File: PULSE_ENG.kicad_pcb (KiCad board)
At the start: 4 copper layers, 142 parts, among them IC1 TPS7B8733QDDARQ1, IC2 TPS7B8750QDDARQ1, IC28 INA226AIDGSR, IC29 TPS25940ARVCR, IC30 TPS25940ARVCR, IC31 INA226AIDGSR, J10 Screw_Terminal_01x01, J11 Screw_Terminal_01x01, J8 Screw_Terminal_01x04, J9 Screw_Terminal_01x06, U1 ATSAMD21J17D-M, U2 LT6108IMS8-1-TRPBF, U3 LM139ADRG4, U4 EPC2152, U5 LT6108IMS8-1-TRPBF

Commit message: Final addings
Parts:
- J11: value Screw_Terminal_01x01 -> Screw_Terminal_01x04; footprint TerminalBlock_Phoenix:TerminalBlock_Phoenix_MKDS-1,5-2-5.08_1x02_P5.08mm_Horizontal -> TerminalBlock_Phoenix:TerminalBlock_Phoenix_MKDS-1,5-4-5.08_1x04_P5.08mm_Horizontal
- moved J11 43.1 mm to (172.0, 61.4)
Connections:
- C3 pad 1: /3.3V -> VDDIN
- C4 pad 1: /3.3V -> VDDIN
- C8 pad 1: Net-(U4-Vdd12F) -> Net-(J11-Pin_3)
- J11 pad 1: /Vout_BUCK -> 12V_1
- J11 pad 2: GND -> /Vout_BUCK
- U1 pad 55: /3.3V -> VDDCORE
- U1 pad 56: /3.3V -> VDDIN
- U4 pad 1: Net-(U4-Vdd12F) -> Net-(J11-Pin_3)
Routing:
- net 12V_1: track 26.5 -> 131.8 mm, vias 3 -> 4
- net Net-(J11-Pin_3): track 0.00 -> 94.6 mm, vias 0 -> 2
- net /Vout_BUCK: track 166.5 -> 207.9 mm
- net Net-(U4-Vdd12F): track 10.7 -> 0.00 mm
- net GND: vias 33 -> 34
- net (no net): vias 1 -> 0
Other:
- board text added: "BUCK pins"
- board text added: "PCU (EPS V4.0) JAN2026 Tom Gourru-Bourgeois"
- board text removed: "BUCK BYPASS Pin"

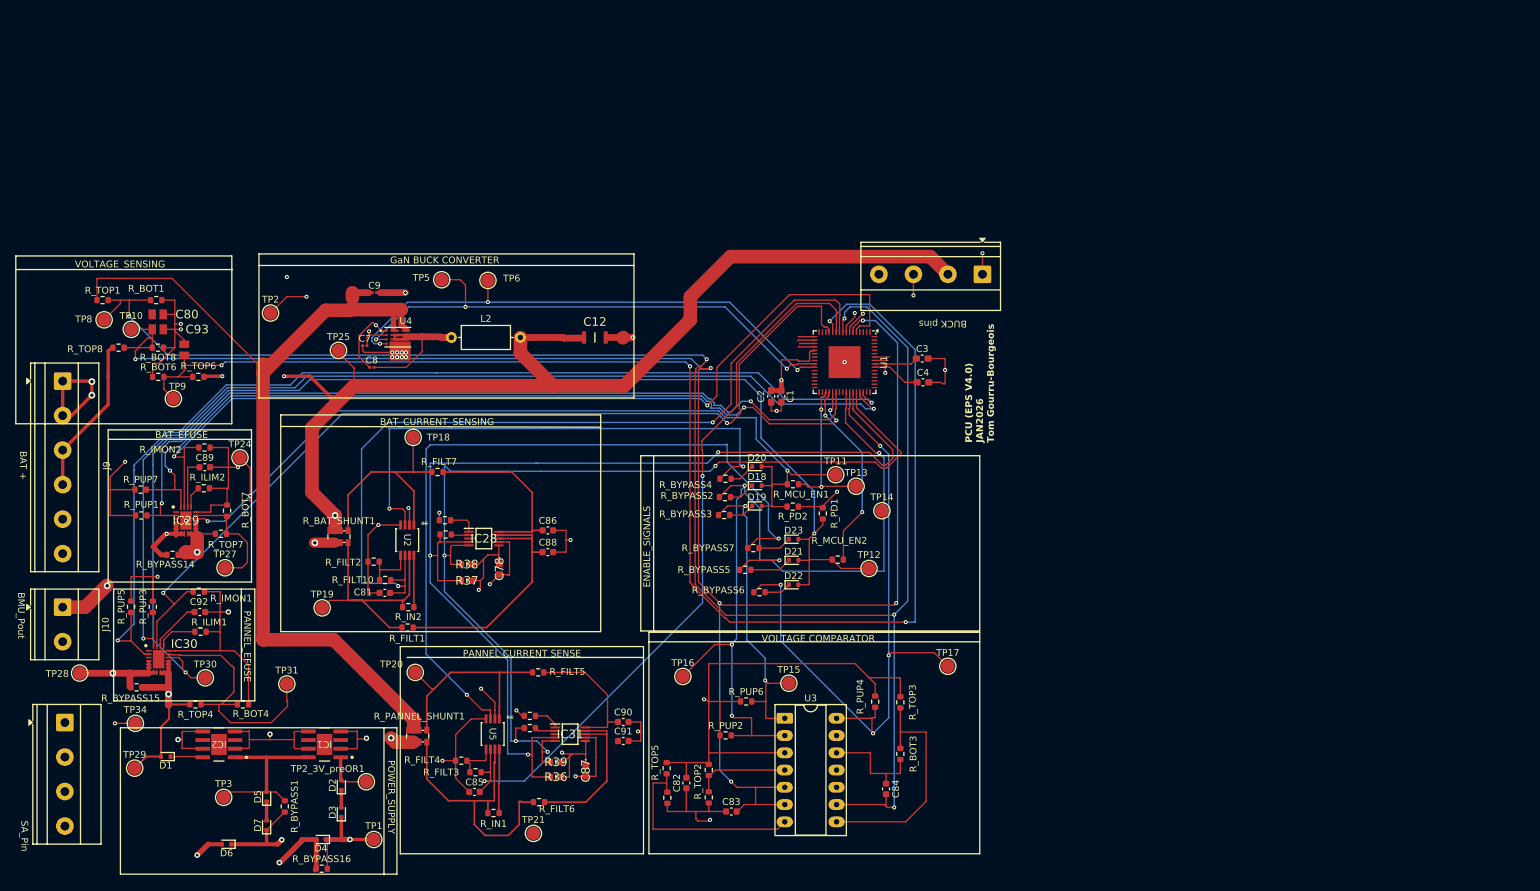
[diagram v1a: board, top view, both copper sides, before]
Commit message: changed 90deg traces, added est logo
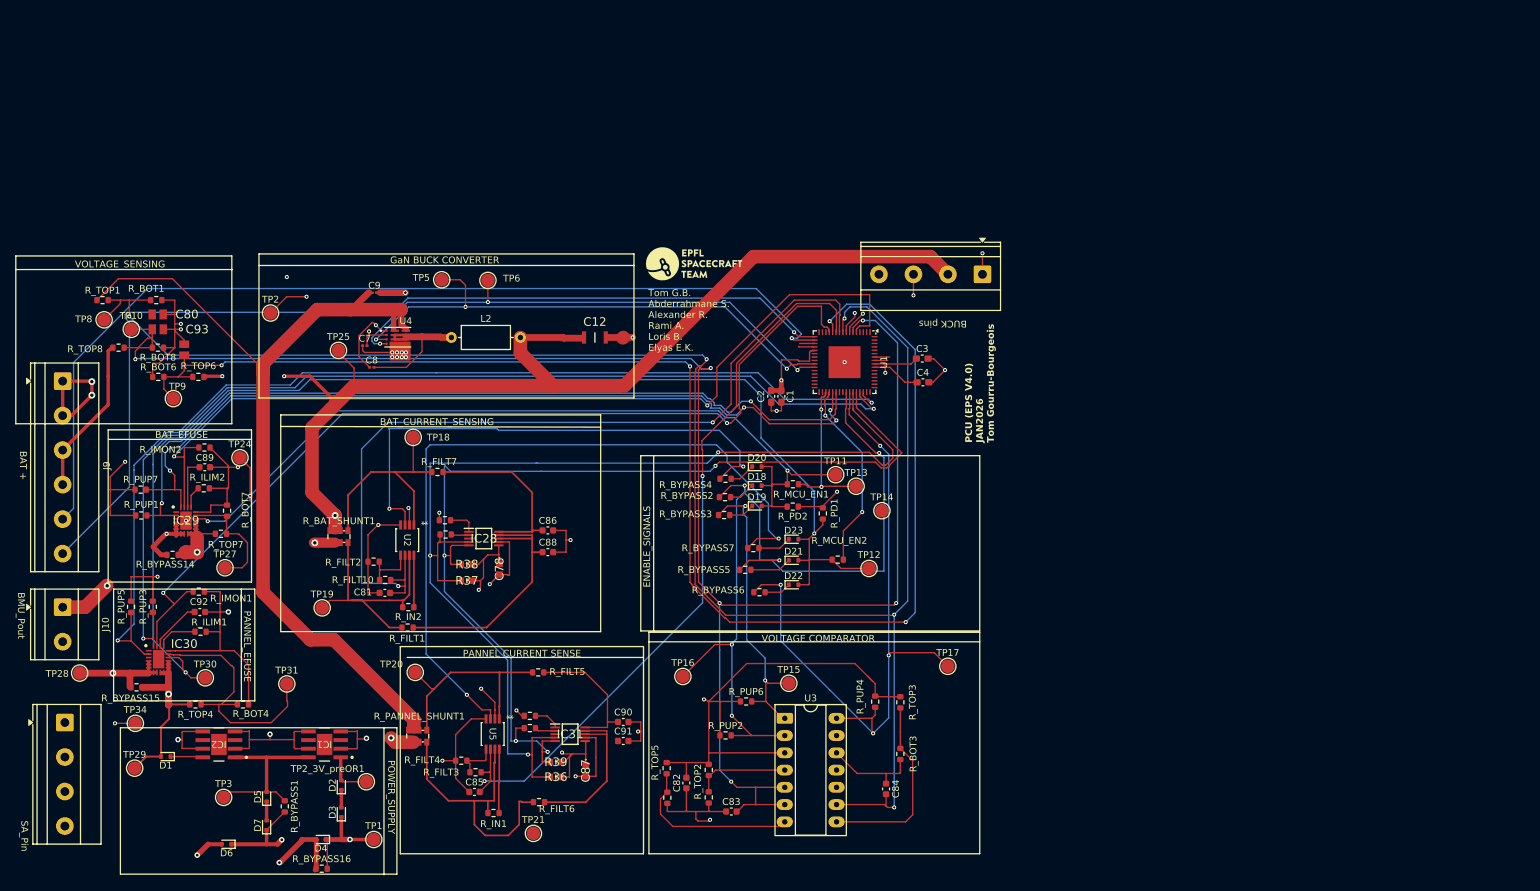
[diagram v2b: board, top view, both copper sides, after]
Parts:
- added G***: LOGO, PULSE_Library:EST_logo_footprint, F.Cu at (129.6, 59.8)
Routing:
- net /HEATER_SWITCH: track 2.40 -> 144.4 mm, vias 0 -> 1
- net /POWER_SWITCH: track 2.54 -> 143.3 mm, vias 0 -> 1
- net /3.3V: track 579.6 -> 569.7 mm
- net /V_pannel_protected: track 138.8 -> 132.0 mm
- net Net-(U3-3IN-): track 34.4 -> 28.1 mm
- net GND: track 282.4 -> 276.6 mm
- net Net-(U3-1IN+): track 31.5 -> 25.9 mm
- net VDDIN: track 0.00 -> 3.34 mm
- net /Vout_BUCK: track 207.9 -> 205.9 mm
- net /PCU_Control/BAT_OVC: track 78.2 -> 76.3 mm
- net /BAT_EFUSE_EN: track 131.5 -> 129.7 mm
- net /BAT_OVP_FLAG: track 129.1 -> 127.6 mm
- net /BAT_UVP_FLAG: track 45.8 -> 44.5 mm
- net /PCU_Control/PANNEL_OVC: track 111.5 -> 110.7 mm
- net /VCHG_RAIL_SENSE: track 212.6 -> 211.7 mm
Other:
- board text added: "Tom G.B. Abderrahmane S. Alexander R. Rami A. Loris B. Elyas E.K."

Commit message: Modofications asked and BOM
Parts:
- D3: value 1N4148WT -> 1N5711; footprint Diode_SMD:D_SOD-523 -> Diode_THT:D_DO-35_SOD27_P7.62mm_Horizontal
- L2: footprint Inductor_THT:L_Axial_L7.0mm_D3.3mm_P10.16mm_Horizontal_Fastron_MICC -> Inductor_SMD:L_0603_1608Metric
- moved R_IN1 17.9 mm to (92.2, 124.6), turned to 90 degrees
- moved TP21 17.6 mm to (90.2, 135.7)
- moved R_IN2 16.8 mm to (80.4, 95.2), turned to 90 degrees
- moved R_FILT1 15.7 mm to (96.7, 100.8), turned to 180 degrees
- moved C81 14.9 mm to (82.8, 93.5), turned to 180 degrees
- moved C85 14.1 mm to (94.5, 123.8), turned to 180 degrees
- moved C88 11.7 mm to (96.4, 103.7), turned to -90 degrees
- moved C86 11.6 mm to (96.6, 97.4)
- moved R_FILT10 11.3 mm to (82.8, 95.2), turned to 180 degrees
- moved R_FILT7 10.1 mm to (96.7, 99.3), turned to 180 degrees
- moved R_FILT3 9.83 mm to (94.5, 125.3), turned to 180 degrees
- moved C91 9.80 mm to (109.6, 132.5)
- moved C90 9.61 mm to (109.5, 126.8)
- moved R_FILT5 9.36 mm to (109.5, 128.9), turned to 180 degrees
- moved R_FILT2 9.32 mm to (86.2, 95.2), turned to 180 degrees
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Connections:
- C1 pad 1: VDDIN -> VDDIO
- C2 pad 1: VDDIN -> VDDIO
- C3 pad 1: VDDIN -> VDDIO
- C4 pad 1: VDDIN -> VDDIO
- C82 pad 1: VDDIN -> VDDIO
- C87 pad 1: VDDIN -> VDDIO
- D3 pad 1: VDDIN -> /5V
- D3 pad 2: Net-(D2-K) -> Net-(D3-A)
- D4 pad 1: VDDIN -> VDDIO
- D5 pad 1: Net-(D5-K) -> Net-(D3-A)
- IC31 pad 6: VDDIN -> VDDIO
- R36 pad 2: VDDIN -> VDDIO
- R39 pad 2: VDDIN -> VDDIO
- R_BYPASS16 pad 2: VDDIN -> VDDIO
- R_PUP2 pad 1: VDDIN -> VDDIO
- R_PUP3 pad 2: VDDIN -> VDDIO
- R_PUP4 pad 2: VDDIN -> VDDIO
- R_PUP5 pad 2: VDDIN -> VDDIO
- R_PUP6 pad 1: VDDIN -> VDDIO
- R_TOP2 pad 2: VDDIN -> VDDIO
- R_TOP3 pad 2: VDDIN -> VDDIO
- R_TOP5 pad 2: VDDIN -> VDDIO
- TP1 pad 1: VDDIN -> VDDIO
- U1 pad 21: VDDIN -> VDDIO
- U1 pad 56: VDDIN -> VDDIO
- U1 pad 8: VDDIN -> VDDIO
- U2 pad 2: VDDIN -> VDDIO
- U3 pad 3: VDDIN -> VDDIO
- U5 pad 2: VDDIN -> VDDIO
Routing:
- net Net-(IC28-IN-): track 38.6 -> 6.61 mm
- net GND: track 276.6 -> 244.7 mm, vias 34 -> 44
- net /I_BAT_ANA: track 123.7 -> 100.6 mm
- net Net-(IC28-IN+): track 26.7 -> 4.10 mm
- net Net-(IC31-IN+): track 20.4 -> 2.13 mm
- net Net-(IC31-IN-): track 24.2 -> 6.15 mm
- net /I_PANNEL_ANA: track 111.6 -> 95.8 mm
- net Net-(U5-SENSEHI): track 9.45 -> 0.00 mm
- net /3.3V: track 569.7 -> 560.3 mm, vias 11 -> 12
- net /Vout_BUCK: track 205.9 -> 214.4 mm
- net /PCU_Control/PANNEL_OVC: track 110.7 -> 117.9 mm
- net /BAT_SHUNT_IN: track 38.0 -> 44.9 mm, vias 0 -> 4
- net Net-(U2-SENSEHI): track 7.64 -> 1.86 mm
- net /PANNEL_SHUNT_IN: track 43.3 -> 37.8 mm, vias 0 -> 4
- net SCL2: track 149.8 -> 144.6 mm, vias 4 -> 6
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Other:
- board outline added: 146.7 x 93.9 mm

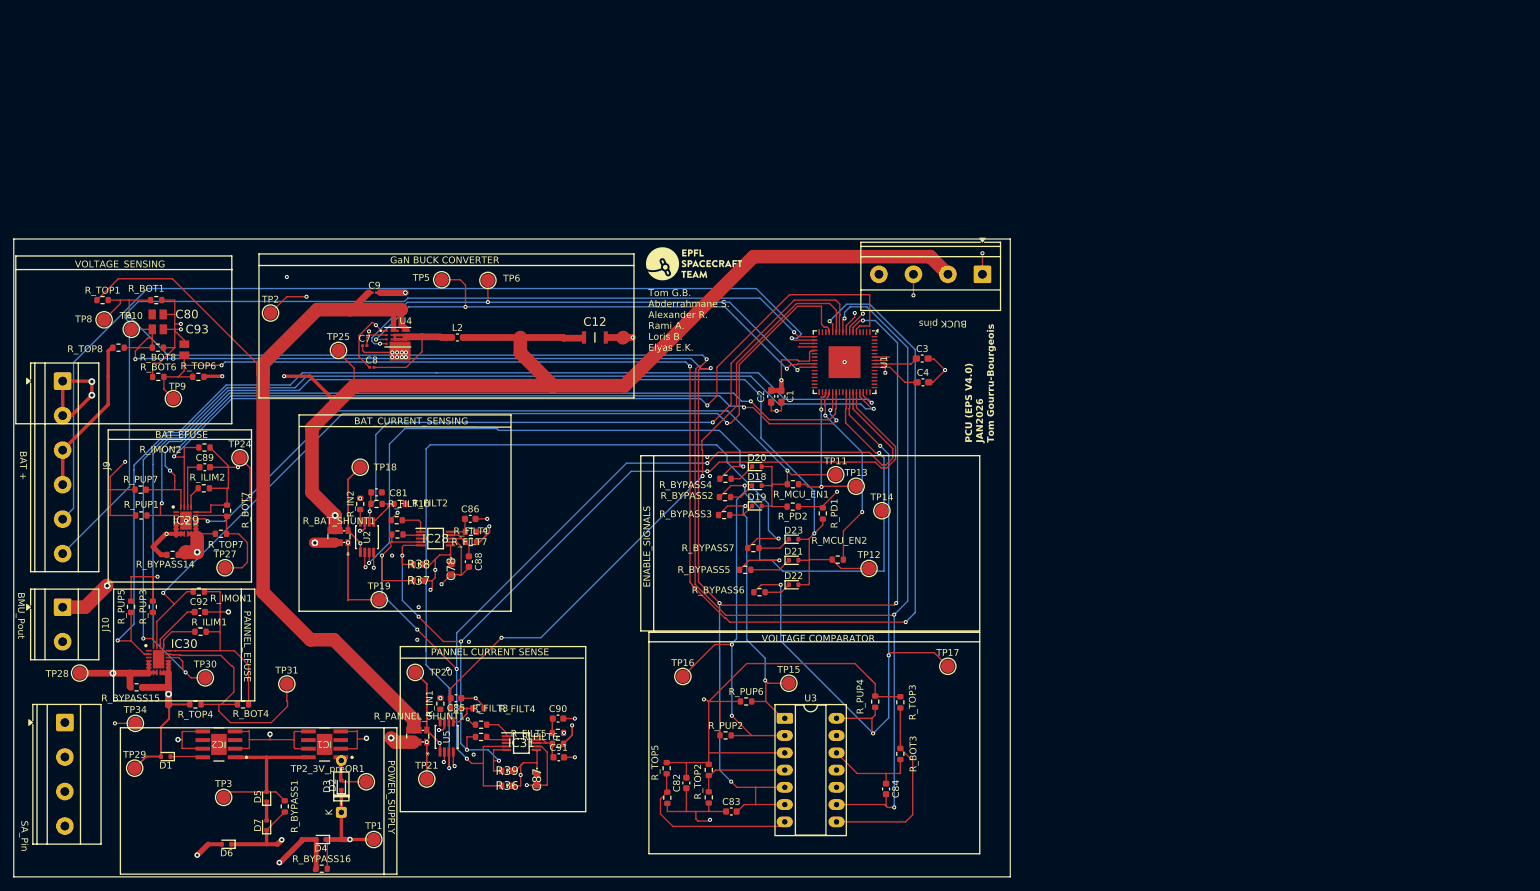
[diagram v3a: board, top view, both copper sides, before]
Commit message: changed mcu power suppl
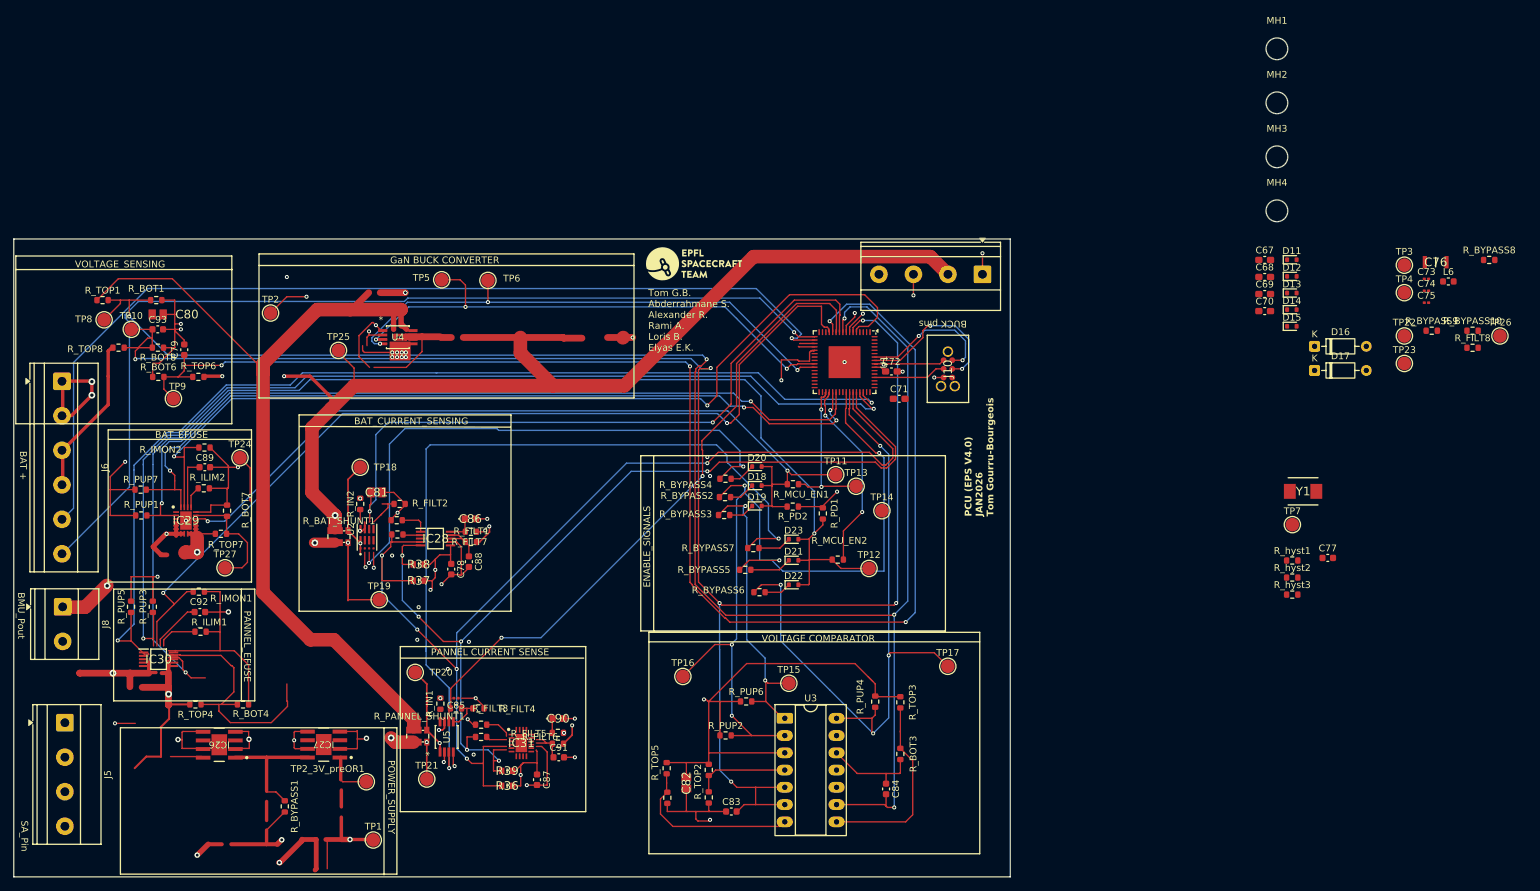
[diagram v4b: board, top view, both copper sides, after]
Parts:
- removed C1, C4: 100nF, Capacitor_SMD:C_0603_1608Metric_Pad1.08x0.95mm_HandSolder
- removed C12: C3216X8L1E106K160AE, PULSE_Library:CAPC3216X180N
- removed C2, C3: 10uF, Capacitor_SMD:C_0603_1608Metric_Pad1.08x0.95mm_HandSolder
- removed C7, C8: 100nF, Capacitor_SMD:C_0201_0603Metric
- removed C9: 4.7uF, Capacitor_SMD:C_0201_0603Metric
- removed D1, D2, D4, D5, D6, D7: 1N4148WT, Diode_SMD:D_SOD-523
- removed D3: 1N5711, Diode_THT:D_DO-35_SOD27_P7.62mm_Horizontal
- removed IC1: TPS7B8733QDDARQ1, PULSE_Library:DDA0008J-IPC_B
- removed IC2: TPS7B8750QDDARQ1, PULSE_Library:DDA0008J-IPC_B
- removed J9: Screw_Terminal_01x06, TerminalBlock_Phoenix:TerminalBlock_Phoenix_MKDS-1,5-6-5.08_1x06_P5.08mm_Horizontal
- removed L2: 47, Inductor_SMD:L_0603_1608Metric
- removed R_BYPASS14, R_BYPASS15, R_BYPASS16: 0, Resistor_SMD:R_0603_1608Metric
- removed R_FILT10: 402, Resistor_SMD:R_0603_1608Metric
- removed TP28: P_Vout_Protected, TestPoint:TestPoint_Pad_D2.0mm
- removed TP29: PVin, TestPoint:TestPoint_Pad_D2.0mm
- removed TP30: eFuse_EN, TestPoint:TestPoint_Pad_D2.0mm
- removed TP31: eFuse_OVP, TestPoint:TestPoint_Pad_D2.0mm
- removed TP34: GND, TestPoint:TestPoint_Pad_D2.0mm
- added C67: 10uF, Capacitor_SMD:C_0603_1608Metric_Pad1.08x0.95mm_HandSolder, F.Cu at (213.5, 59.3)
- added C68: 10uF, Capacitor_SMD:C_0603_1608Metric_Pad1.08x0.95mm_HandSolder, F.Cu at (213.5, 61.8)
- added C69: 100nF, Capacitor_SMD:C_0603_1608Metric_Pad1.08x0.95mm_HandSolder, F.Cu at (213.5, 64.3)
- added C70: 100nF, Capacitor_SMD:C_0603_1608Metric_Pad1.08x0.95mm_HandSolder, F.Cu at (213.5, 66.8)
- added C71: 100nF, Capacitor_SMD:C_0603_1608Metric_Pad1.08x0.95mm_HandSolder, F.Cu at (159.7, 79.7)
- added C72: 1uF, Capacitor_SMD:C_0603_1608Metric_Pad1.08x0.95mm_HandSolder, F.Cu at (158.6, 75.7)
- added C73: 100nF, Capacitor_SMD:C_0201_0603Metric, F.Cu at (237.4, 62.1)
- added C74: 100nF, Capacitor_SMD:C_0201_0603Metric, F.Cu at (237.4, 63.8)
- added C75: 4.7uF, Capacitor_SMD:C_0201_0603Metric, F.Cu at (237.4, 65.6)
- added C76: C3216X8L1E106K160AE, PULSE_Library:CAPC3216X180N, F.Cu at (238.7, 59.6)
- added C77: 100nF, Capacitor_SMD:C_0603_1608Metric, F.Cu at (222.8, 103.2)
- added D11: 1N4148WT, Diode_SMD:D_SOD-523, F.Cu at (217.5, 59.3)
- added D12: 1N4148WT, Diode_SMD:D_SOD-523, F.Cu at (217.5, 61.7)
- added D13: 1N4148WT, Diode_SMD:D_SOD-523, F.Cu at (217.5, 64.2)
- added D14: 1N4148WT, Diode_SMD:D_SOD-523, F.Cu at (217.5, 66.6)
- added D15: 1N4148WT, Diode_SMD:D_SOD-523, F.Cu at (217.5, 69.1)
- added D16: 1N5711, Diode_THT:D_DO-35_SOD27_P7.62mm_Horizontal, F.Cu at (220.9, 72.0)
- added D17: 1N5711, Diode_THT:D_DO-35_SOD27_P7.62mm_Horizontal, F.Cu at (220.9, 75.6)
- added IC26: TPS7B8750QDDARQ1, PULSE_Library:DDA0008J-IPC_B, F.Cu at (59.6, 130.7)
- added IC27: TPS7B8733QDDARQ1, PULSE_Library:DDA0008J-IPC_B, F.Cu at (75.0, 130.6)
- added J5: Screw_Terminal_01x04, TerminalBlock_Phoenix:TerminalBlock_Phoenix_MKDS-1,5-4-5.08_1x04_P5.08mm_Horizontal, F.Cu at (36.9, 127.4)
- added J6: Screw_Terminal_01x06, TerminalBlock_Phoenix:TerminalBlock_Phoenix_MKDS-1,5-6-5.08_1x06_P5.08mm_Horizontal, F.Cu at (36.5, 77.1)
- added L6: 47, Inductor_SMD:L_0603_1608Metric, F.Cu at (240.6, 62.5)
- added MH1: MountingHole, MountingHole:MountingHole_3.2mm_M3, F.Cu at (215.3, 28.2)
- added MH2: MountingHole, MountingHole:MountingHole_3.2mm_M3, F.Cu at (215.3, 36.2)
- added MH3: MountingHole, MountingHole:MountingHole_3.2mm_M3, F.Cu at (215.3, 44.1)
- added MH4: MountingHole, MountingHole:MountingHole_3.2mm_M3, F.Cu at (215.3, 52.1)
- added R_BYPASS10: 0, Resistor_SMD:R_0603_1608Metric, F.Cu at (244.1, 69.7)
- added R_BYPASS8: 0, Resistor_SMD:R_0603_1608Metric, F.Cu at (246.6, 59.3)
- added R_BYPASS9: 0, Resistor_SMD:R_0603_1608Metric, F.Cu at (238.1, 69.7)
- added R_FILT8: 10, Resistor_SMD:R_0603_1608Metric, F.Cu at (244.1, 72.2)
- added R_hyst1: 1MOhm, Resistor_SMD:R_0603_1608Metric, F.Cu at (217.6, 103.5)
- added R_hyst2: 1MOhm, Resistor_SMD:R_0603_1608Metric, F.Cu at (217.6, 106.0)
- added R_hyst3: 1MOhm, Resistor_SMD:R_0603_1608Metric, F.Cu at (217.6, 108.5)
- added TP22: eFUSE_OVP, TestPoint:TestPoint_Pad_D2.0mm, F.Cu at (234.1, 70.5)
- added TP23: Buck_out, TestPoint:TestPoint_Pad_D2.0mm, F.Cu at (234.1, 74.5)
- added TP26: PVin, TestPoint:TestPoint_Pad_D2.0mm, F.Cu at (248.2, 70.5)
- added TP4: PWM_H, TestPoint:TestPoint_Pad_D2.0mm, F.Cu at (234.1, 64.1)
- added TP7: BAT_OVP, TestPoint:TestPoint_Pad_D2.0mm, F.Cu at (217.6, 98.2)
- added Y1: AMDLA4020S-220MT, PULSE_Library:INDPM4440X200N, F.Cu at (219.2, 93.3)
- C78, C87: value 0.1μF -> 100nF; footprint PULSE_Library:C0603 -> Capacitor_SMD:C_0603_1608Metric
- C79, C93: value 10nF -> 100nF; footprint PULSE_Library:CAPC2012X145N -> Capacitor_SMD:C_0603_1608Metric
- C81, C82: value 100nF -> 10nF; footprint Capacitor_SMD:C_0603_1608Metric -> PULSE_Library:CAPC2012X145N
- C85: value 100nF -> C; footprint Capacitor_SMD:C_0603_1608Metric -> Capacitor_SMD:C_0201_0603Metric
- C86, C90: value 100nF -> 0.1μF; footprint Capacitor_SMD:C_0603_1608Metric -> PULSE_Library:C0603
- IC30: value TPS25940ARVCR -> INA226AIDGSR; footprint PULSE_Library:QFN50P300X400X80-21N -> PULSE_Library:SOP50P490X110-10N
- IC31: value INA226AIDGSR -> TPS25940ARVCR; footprint PULSE_Library:SOP50P490X110-10N -> PULSE_Library:QFN50P300X400X80-21N
- J10: value Screw_Terminal_01x01 -> TC2030-MCP; footprint TerminalBlock_Phoenix:TerminalBlock_Phoenix_MKDS-1,5-2-5.08_1x02_P5.08mm_Horizontal -> PULSE_Library:TC2030IDCNL
- J8: value Screw_Terminal_01x04 -> Screw_Terminal_01x01; footprint TerminalBlock_Phoenix:TerminalBlock_Phoenix_MKDS-1,5-4-5.08_1x04_P5.08mm_Horizontal -> TerminalBlock_Phoenix:TerminalBlock_Phoenix_MKDS-1,5-2-5.08_1x02_P5.08mm_Horizontal
- R_BOT4: value 100k -> 180k
- R_BOT8: value 180k -> 100k
- R_FILT1: value 10 -> 402
- R_ILIM1: value 24k -> 16.9k
- R_ILIM2: value 16.9k -> 24k
- R_TOP1: value 680k -> 247k
- R_TOP4: value 681 -> 680k
- R_TOP5: value 247k -> 680k
- R_TOP8: value 680k -> 681
- TP10: value VBAT_SENSE -> VPANNEL_SENSE
- TP11: value BAT_EFUSE_EN -> PANNEL_SHUNT_OUT
- TP12: value PANNEL_EFUSE_EN -> VCHG_RAIL_SENSE
- TP13: value MCU_BAT_EFUSE_EN -> VBAT_SENSE
- TP14: value MCU_PANNEL_EFUSE_EN -> BAT_SHUNT_OUT
- TP15: value BAT_UVP -> BAT_EFUSE_EN
- TP16: value BAT_OVP -> PANNEL_EFUSE_EN
- TP17: value PANNEL_OVP -> MCU_BAT_EFUSE_EN
- TP18: value BAT_SHUNT_OUT -> MCU_PANNEL_EFUSE_EN
- TP2: value 12Vin_buck -> GND
- TP20: value PANNEL_SHUNT_OUT -> PANNEL_SHUNT_IN
- TP21: value PANNEL_SHUNT_IN -> eFUSE_EN
- TP24: value eFUSE_EN -> eFuse_OVP
- TP25: value Buck_out -> eFuse_EN
- TP27: value eFUSE_OVP -> P_Vout_Protected
- TP3: value 5V_preOR -> 12Vin_buck
- TP5: value PWM_H -> PWM_L
- TP6: value PWM_L -> Buck_out
- TP8: value VPANNEL_SENSE -> BAT_UVP
- TP9: value VCHG_RAIL_SENSE -> PANNEL_OVP
- U2: value LT6108IMS8-1-TRPBF -> EPC2152; footprint PULSE_Library:MSOP-8_MS_LIT -> PULSE_Library:VREG_EPC2152ENGRT
- U4: value EPC2152 -> LT6108IMS8-1-TRPBF; footprint PULSE_Library:VREG_EPC2152ENGRT -> PULSE_Library:MSOP-8_MS_LIT
- moved TP3 190.6 mm to (234.1, 60.1)
- moved J10 135.0 mm to (166.9, 75.3)
- moved J8 17.0 mm to (36.6, 110.4)
- moved TP1 0.11 mm to (82.3, 144.7)
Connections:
- C78 pad 1: /3.3V -> GND
- C78 pad 2: GND -> /VBAT_SENSE
- C79 pad 1: /VCHG_RAIL_SENSE -> GND
- C79 pad 2: GND -> /VPANNEL_SENSE
- C81 pad 1: GND -> /VCHG_RAIL_SENSE
- C81 pad 2: /I_BAT_ANA -> GND
- C82 pad 1: VDDIO -> /VBAT_SENSE
- C83 pad 2: /VBAT_SENSE -> /I_PANNEL_ANA
- C84 pad 2: /VPANNEL_SENSE -> /I_BAT_ANA
- C85 pad 1: GND -> /5V
- C85 pad 2: /I_PANNEL_ANA -> GND
- C86 pad 1: Net-(IC28-IN+) -> /3V3
- C87 pad 1: VDDIO -> Net-(IC28-IN+)
- C90 pad 1: Net-(IC31-IN+) -> /3V3
- C91 pad 1: Net-(IC31-IN-) -> Net-(IC30-IN+)
- C92 pad 1: GND -> Net-(IC30-IN-)
- C92 pad 2: Net-(IC30-DVDT) -> GND
- C93 pad 1: /VBAT_SENSE -> GND
- C93 pad 2: GND -> Net-(IC31-DVDT)
- IC28 pad 6: /3.3V -> /3V3
- IC30 pad 1: unconnected-(IC30-DEVSLP-Pad1) -> Net-(IC30-A1)
- IC30 pad 10: /TEST_Pin_SA -> Net-(IC30-IN+)
- IC30 pad 2: /PAN_EFUSE_PGOOD -> Net-(IC30-A0)
- IC30 pad 4: /Pannel_protection_and_sensing/PV_protected -> SDA2
- IC30 pad 5: /Pannel_protection_and_sensing/PV_protected -> SCL2
- IC30 pad 6: /Pannel_protection_and_sensing/PV_protected -> /3V3
- IC30 pad 7: /Pannel_protection_and_sensing/PV_protected -> GND
- IC30 pad 8: /Pannel_protection_and_sensing/PV_protected -> Net-(IC30-IN-)
- IC30 pad 9: /TEST_Pin_SA -> Net-(IC30-IN-)
- IC31 pad 1: Net-(IC31-A1) -> unconnected-(IC31-DEVSLP-Pad1)
- IC31 pad 10: Net-(IC31-IN+) -> /TEST_Pin_SA
- IC31 pad 2: Net-(IC31-A0) -> /PAN_EFUSE_PGOOD
- IC31 pad 4: SDA2 -> /Pannel_protection_and_sensing/PV_protected
- IC31 pad 5: SCL2 -> /Pannel_protection_and_sensing/PV_protected
- IC31 pad 6: VDDIO -> /Pannel_protection_and_sensing/PV_protected
- IC31 pad 7: GND -> /Pannel_protection_and_sensing/PV_protected
- IC31 pad 8: Net-(IC31-IN-) -> /Pannel_protection_and_sensing/PV_protected
- IC31 pad 9: Net-(IC31-IN-) -> /TEST_Pin_SA
- J10 pad 1: /Battery_protection_and_sensing/P_Vout_Protected -> /3V3
- J10 pad 2: (no net) -> SWDIO
- J8 pad 1: GND -> /Battery_protection_and_sensing/P_Vout_Protected
- J8 pad 2: /TEST_3V_PDU -> (no net)
- R36 pad 2: VDDIO -> /3V3
- R37 pad 1: SDA2 -> SCL2
- R37 pad 2: /3.3V -> /3V3
- R38 pad 1: SCL2 -> SDA2
- R38 pad 2: /3.3V -> /3V3
- R39 pad 2: VDDIO -> /3V3
- R_ADD_CONFIG1 pad 1: SDA2 -> GND
- R_ADD_CONFIG1 pad 2: Net-(IC28-A0) -> Net-(IC28-A1)
- R_ADD_CONFIG2 pad 1: GND -> SDA2
- R_ADD_CONFIG2 pad 2: Net-(IC31-A1) -> Net-(IC28-A0)
- R_ADD_CONFIG3 pad 1: SCL2 -> GND
- R_ADD_CONFIG3 pad 2: Net-(IC31-A0) -> Net-(IC30-A1)
- R_ADD_CONFIG4 pad 1: GND -> SCL2
- R_ADD_CONFIG4 pad 2: Net-(IC28-A1) -> Net-(IC30-A0)
- R_BOT1 pad 2: /VPANNEL_SENSE -> Net-(U3-1IN+)
- R_BOT4 pad 1: Net-(IC30-OVP) -> GND
- R_BOT4 pad 2: GND -> /VPANNEL_SENSE
- R_BOT5 pad 2: Net-(U3-1IN+) -> /VCHG_RAIL_SENSE
- R_BOT6 pad 2: /VCHG_RAIL_SENSE -> /VBAT_SENSE
- R_BOT8 pad 1: GND -> Net-(IC31-OVP)
- R_BOT8 pad 2: /VBAT_SENSE -> GND
- R_BYPASS2 pad 1: /BAT_OVP_FLAG -> /TEST_3V_PDU
- R_BYPASS2 pad 2: Net-(D18-K) -> /3V3
- R_BYPASS3 pad 1: /BAT_UVP_FLAG -> /BAT_OVP_FLAG
- R_BYPASS3 pad 2: Net-(D19-K) -> Net-(D18-K)
- R_BYPASS4 pad 1: /PCU_Control/BAT_OVC -> /BAT_UVP_FLAG
- R_BYPASS4 pad 2: Net-(D20-K) -> Net-(D19-K)
- R_BYPASS5 pad 1: /BAT_OVP_FLAG -> /PCU_Control/BAT_OVC
- R_BYPASS5 pad 2: Net-(D21-K) -> Net-(D20-K)
- R_BYPASS6 pad 1: /PANNEL_OVP_FLAG -> /BAT_OVP_FLAG
- R_BYPASS6 pad 2: Net-(D22-K) -> Net-(D21-K)
- R_BYPASS7 pad 1: /PCU_Control/PANNEL_OVC -> /PANNEL_OVP_FLAG
- R_BYPASS7 pad 2: Net-(D23-K) -> Net-(D22-K)
- R_FILT1 pad 1: /BAT_SHUNT_IN -> Net-(U4-INC)
- R_FILT1 pad 2: Net-(IC28-IN-) -> /I_PANNEL_ANA
- R_FILT2 pad 2: Net-(U2-INC) -> Net-(U4-INC)
- R_FILT3 pad 2: /I_PANNEL_ANA -> /I_BAT_ANA
- R_FILT5 pad 1: /PANNEL_SHUNT_OUT -> /BAT_SHUNT_OUT
- R_FILT5 pad 2: Net-(IC31-IN+) -> Net-(IC28-IN+)
- R_FILT6 pad 1: /PANNEL_SHUNT_IN -> /BAT_SHUNT_IN
- R_FILT6 pad 2: Net-(IC31-IN-) -> Net-(IC28-IN-)
- R_FILT7 pad 1: /BAT_SHUNT_OUT -> /PANNEL_SHUNT_OUT
- R_FILT7 pad 2: Net-(IC28-IN+) -> Net-(IC30-IN+)
- R_ILIM1 pad 1: Net-(IC30-ILIM) -> Net-(IC29-ILIM)
- R_ILIM2 pad 1: Net-(IC29-ILIM) -> Net-(IC31-ILIM)
- R_IMON1 pad 2: /PAN_EFUSE_IMON -> /BAT_EFUSE_IMON
- R_IMON2 pad 2: /BAT_EFUSE_IMON -> /PAN_EFUSE_IMON
- R_IN1 pad 1: Net-(U5-SENSEHI) -> Net-(U4-SENSEHI)
- R_IN2 pad 1: Net-(U2-SENSEHI) -> Net-(U5-SENSEHI)
- R_PD1 pad 2: /PANNEL_EFUSE_EN -> /BAT_EFUSE_EN
- R_PD2 pad 2: /BAT_EFUSE_EN -> /PANNEL_EFUSE_EN
- R_PUP1 pad 1: /BAT_EFUSE_PGOOD -> /3V3
- R_PUP1 pad 2: /3.3V -> /BAT_UVP_FLAG
- R_PUP2 pad 1: VDDIO -> /3V3
- R_PUP3 pad 1: /PAN_EFUSE_FLT -> /PANNEL_OVP_FLAG
- R_PUP3 pad 2: VDDIO -> /3V3
- R_PUP4 pad 1: /PANNEL_OVP_FLAG -> /BAT_EFUSE_FLT
- R_PUP4 pad 2: VDDIO -> /3V3
- R_PUP5 pad 1: /PAN_EFUSE_PGOOD -> /BAT_EFUSE_PGOOD
- R_PUP5 pad 2: VDDIO -> /3V3
- R_PUP6 pad 1: VDDIO -> /PAN_EFUSE_FLT
- R_PUP6 pad 2: /BAT_UVP_FLAG -> /3V3
- R_PUP7 pad 1: /BAT_EFUSE_FLT -> /PAN_EFUSE_PGOOD
- R_PUP7 pad 2: /3.3V -> /3V3
- R_TOP1 pad 1: /V_pannel_protected -> Net-(U3-1IN+)
- R_TOP1 pad 2: /VPANNEL_SENSE -> /3V3
- R_TOP2 pad 2: VDDIO -> /3V3
- R_TOP3 pad 2: VDDIO -> /3V3
- R_TOP4 pad 1: /TEST_Pin_SA -> /V_pannel_protected
- R_TOP4 pad 2: Net-(IC30-OVP) -> /VPANNEL_SENSE
- R_TOP5 pad 1: Net-(U3-1IN+) -> /Vout_BUCK
- R_TOP5 pad 2: VDDIO -> /VCHG_RAIL_SENSE
- R_TOP6 pad 1: /Vout_BUCK -> /Vbat
- R_TOP6 pad 2: /VCHG_RAIL_SENSE -> /VBAT_SENSE
- R_TOP8 pad 1: /Vbat -> /TEST_Pin_SA
- R_TOP8 pad 2: /VBAT_SENSE -> Net-(IC31-OVP)
- TP1 pad 1: VDDIO -> /3V3
- TP10 pad 1: /VBAT_SENSE -> /VPANNEL_SENSE
- TP11 pad 1: /BAT_EFUSE_EN -> /PANNEL_SHUNT_OUT
- TP12 pad 1: /PANNEL_EFUSE_EN -> /VCHG_RAIL_SENSE
- TP13 pad 1: /MCU_BAT_EFUSE_EN -> /VBAT_SENSE
- TP14 pad 1: /MCU_PANNEL_EFUSE_EN -> /BAT_SHUNT_OUT
- TP15 pad 1: /BAT_UVP_FLAG -> /BAT_EFUSE_EN
- TP16 pad 1: /BAT_OVP_FLAG -> /PANNEL_EFUSE_EN
- TP17 pad 1: /PANNEL_OVP_FLAG -> /MCU_BAT_EFUSE_EN
- TP18 pad 1: /BAT_SHUNT_OUT -> /MCU_PANNEL_EFUSE_EN
- TP2 pad 1: 12V_1 -> GND
- TP20 pad 1: /PANNEL_SHUNT_OUT -> /PANNEL_SHUNT_IN
- TP21 pad 1: /PANNEL_SHUNT_IN -> /BAT_EFUSE_EN
- TP24 pad 1: /BAT_EFUSE_EN -> Net-(IC31-OVP)
- TP25 pad 1: /Vout_BUCK -> /PANNEL_EFUSE_EN
- TP27 pad 1: Net-(IC29-OVP) -> /Pannel_protection_and_sensing/PV_protected
- TP3 pad 1: /EPS_Power_Supply/5V_LDO -> 12V_1
- TP5 pad 1: /GAN_PWM_H -> /GAN_PWM_L
- TP6 pad 1: /GAN_PWM_L -> /Vout_BUCK
- TP8 pad 1: /VPANNEL_SENSE -> /BAT_UVP_FLAG
- TP9 pad 1: /VCHG_RAIL_SENSE -> /PANNEL_OVP_FLAG
- U1 pad 21: VDDIO -> /3V3
- U1 pad 22: Net-(U1-GND-Pad22) -> GND
- U1 pad 33: Net-(U1-GND-Pad22) -> GND
- U1 pad 34: unconnected-(U1-VDDIO-Pad34) -> /3V3
- U1 pad 47: Net-(U1-GND-Pad22) -> GND
- U1 pad 48: unconnected-(U1-VDDIO-Pad48) -> /3V3
- U1 pad 54: Net-(U1-GND-Pad22) -> GND
- U1 pad 56: VDDIO -> /3V3
- U1 pad 8: VDDIO -> /3V3
- U2 pad 1: /BAT_SHUNT_OUT -> Net-(J11-Pin_3)
- U2 pad 2: VDDIO -> 12V_1
- U2 pad 3: /PCU_Control/BAT_OVC -> /GAN_PWM_H
- U2 pad 4: GND -> /GAN_PWM_L
- U2 pad 5: Net-(U2-INC) -> /V_pannel_protected
- U2 pad 6: /I_BAT_ANA -> Net-(C74-Pad2)
- U2 pad 7: /BAT_SHUNT_IN -> Net-(C74-Pad2)
- U2 pad 8: Net-(U2-SENSEHI) -> GND
- U3 pad 3: VDDIO -> /3V3
- U4 pad 1: Net-(J11-Pin_3) -> /PANNEL_SHUNT_OUT
- U4 pad 2: 12V_1 -> /3V3
- U4 pad 3: /GAN_PWM_H -> /PCU_Control/PANNEL_OVC
- U4 pad 4: /GAN_PWM_L -> GND
- U4 pad 5: /V_pannel_protected -> Net-(U4-INC)
- U4 pad 6: Net-(C8-Pad2) -> /I_PANNEL_ANA
- U4 pad 7: Net-(C8-Pad2) -> /PANNEL_SHUNT_IN
- U4 pad 8: GND -> Net-(U4-SENSEHI)
- U5 pad 1: /PANNEL_SHUNT_OUT -> /BAT_SHUNT_OUT
- U5 pad 2: VDDIO -> /3V3
- U5 pad 3: /PCU_Control/PANNEL_OVC -> /PCU_Control/BAT_OVC
- U5 pad 6: /I_PANNEL_ANA -> /I_BAT_ANA
- U5 pad 7: /PANNEL_SHUNT_IN -> /BAT_SHUNT_IN
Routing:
- net /3.3V: track 560.3 -> 0.00 mm, vias 12 -> 0
- net /3V3: track 0.00 -> 543.7 mm, vias 0 -> 12
- net (no net): track 3.34 -> 93.2 mm, vias 0 -> 3
- net /BAT_UVP_FLAG: track 44.5 -> 125.7 mm, vias 2 -> 4
- net /PCU_Control/BAT_OVC: track 81.1 -> 0.00 mm, vias 2 -> 0
- net Net-(IC30-OVP): track 38.1 -> 0.00 mm
- net /TEST_Pin_SA: track 65.2 -> 88.3 mm
- net /Vbat: track 67.0 -> 43.9 mm
- net SWCLK: track 1.94 -> 23.7 mm, vias 0 -> 2
- net Net-(C8-Pad2): track 21.5 -> 0.00 mm
- net SWDIO: track 2.24 -> 20.2 mm, vias 0 -> 2
- net nRESET: track 0.00 -> 10.7 mm
- net Net-(IC30-DVDT): track 8.26 -> 0.00 mm
- net Net-(C12-Pad1): track 7.97 -> 0.00 mm, vias 3 -> 0
- net /EPS_Power_Supply/5V_LDO: track 25.7 -> 19.0 mm
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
